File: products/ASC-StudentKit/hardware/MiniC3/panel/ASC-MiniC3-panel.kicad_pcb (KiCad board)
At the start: 2 copper layers, 96 x 100 mm, 156 parts, among them J1_1 PUMP, J1_2 PUMP, J1_3 PUMP, J1_4 PUMP, J1_5 CABLE, J1_6 CABLE, J1_7 CABLE, J1_8 CABLE, J3_1 AUX, J3_2 AUX, J3_3 AUX, J3_4 AUX, J4_1 FLOW, J4_2 FLOW, J4_3 FLOW, J4_4 FLOW, J5_1 I2C, J5_2 I2C, J5_3 I2C, J5_4 I2C, J6_1 RELAY 230V, J6_2 RELAY 230V, J6_3 RELAY 230V, J6_4 RELAY 230V, K1_1 HF46F/005-HS1, K1_2 HF46F/005-HS1, K1_3 HF46F/005-HS1, K1_4 HF46F/005-HS1, Q1_1 AO3400A, Q1_2 AO3400A, Q1_3 AO3400A, Q1_4 AO3400A, Q2_1 AO3400A, Q2_2 AO3400A, Q2_3 AO3400A, Q2_4 AO3400A, U1_1 ESP32-C3 Super Mini, U1_2 ESP32-C3 Super Mini, U1_3 ESP32-C3 Super Mini, U1_4 ESP32-C3 Super Mini, U1_5 AHT20, U1_6 AHT20, U1_7 AHT20, U1_8 AHT20, U2_1 DS1307Z+, U2_2 DS1307Z+, U2_3 DS1307Z+, U2_4 DS1307Z+, Y1_1 32.768k 12.5pF, Y1_2 32.768k 12.5pF, Y1_3 32.768k 12.5pF, Y1_4 32.768k 12.5pF

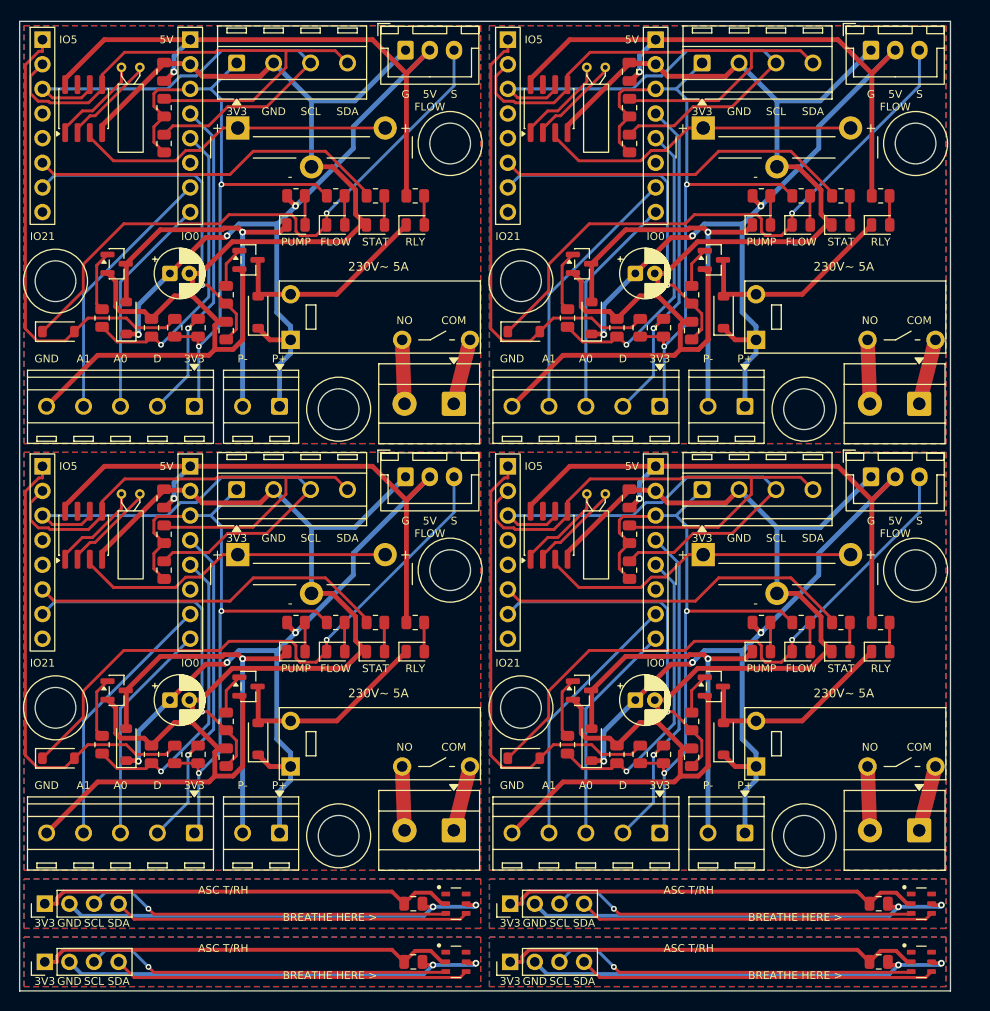
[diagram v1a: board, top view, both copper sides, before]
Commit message: ASC Mini-C3: ULN2003A driver, combo flow connector, assembly markings
- ULN2003A (LCSC C7512) drives the pump (ch 1+2) and the relay (ch 3);
  replaces 2 x AO3400A, 3 x B5819W and 4 resistors, as on FG1
- Flow input: one footprint takes a JST-XH (bench) or a 3.5 mm 3-pole
  screw terminal (FG1 field cable)
- Screw terminals now Phoenix PT-1,5 3.5 mm (KF350 type, library 3D);
  relay output is a pluggable MSTBVA 5.08 header like FG1's
- 1206 LEDs for hand soldering; ref + value labels on every part
  (R3 1K, U3 ULN2003 ...), "1" at IC pin 1, "+" at LED/diode anodes;
  back reads "Agri Sensors and Controls  Oct 2026"
- Re-routed, DRC clean (mains 5 mm), panel and fab regenerated
- Sourcing BOM: 1206 LED and ULN2003A LCSC numbers, CR2032 holder as an
  alternative to the tabbed cell; kit about Rs 967

Co-Authored-By: Claude Opus 5.5 <noreply@anthropic.com>
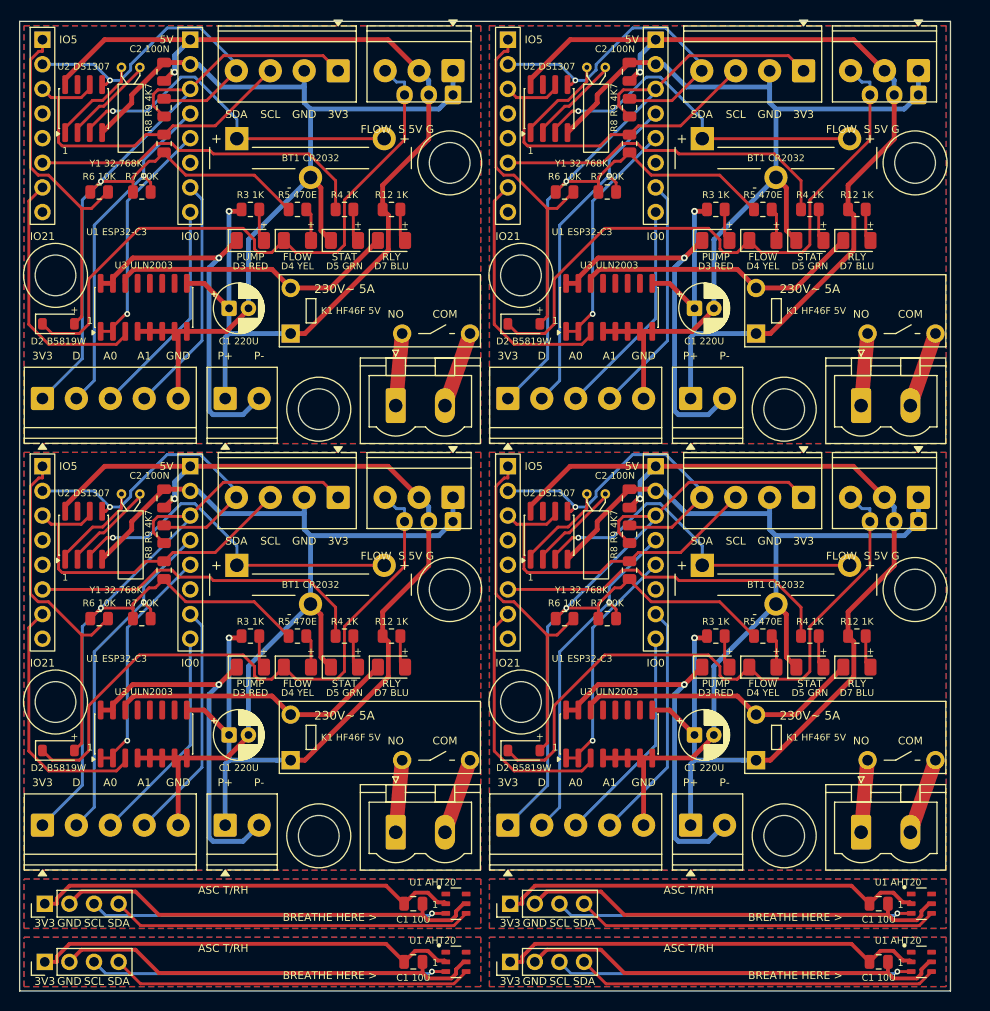
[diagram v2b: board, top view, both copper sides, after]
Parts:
- removed D1_1, D1_2, D1_3, D1_4, D6_1, D6_2, D6_3, D6_4: B5819W, Diode_SMD:D_SOD-123
- removed Q1_1, Q1_2, Q1_3, Q1_4, Q2_1, Q2_2, Q2_3, Q2_4: AO3400A, Package_TO_SOT_SMD:SOT-23
- removed R10_1, R10_2, R10_3, R10_4, R1_1, R1_2, R1_3, R1_4: 100, Resistor_SMD:R_0805_2012Metric
- removed R11_1, R11_2, R11_3, R11_4, R2_1, R2_2, R2_3, R2_4: 100k, Resistor_SMD:R_0805_2012Metric
- added U3_1: ULN2003A, Package_SO:SOIC-16_3.9x9.9mm_P1.27mm, F.Cu at (112.8, 89.5)
- added U3_2: ULN2003A, Package_SO:SOIC-16_3.9x9.9mm_P1.27mm, F.Cu at (160.8, 89.5)
- added U3_3: ULN2003A, Package_SO:SOIC-16_3.9x9.9mm_P1.27mm, F.Cu at (112.8, 133.5)
- added U3_4: ULN2003A, Package_SO:SOIC-16_3.9x9.9mm_P1.27mm, F.Cu at (160.8, 133.5)
- D3_1, D3_2, D3_3, D3_4, D4_1, D4_2, D4_3, D4_4, D5_1, D5_2, D5_3, D5_4, D7_1, D7_2, D7_3, D7_4: footprint LED_SMD:LED_0805_2012Metric -> LED_SMD:LED_1206_3216Metric
- J1_1, J1_2, J1_3, J1_4: footprint TerminalBlock_MetzConnect:TerminalBlock_MetzConnect_Type086_RT03402HBLC_1x02_P3.81mm_Horizontal -> TerminalBlock_Phoenix:TerminalBlock_Phoenix_PT-1,5-2-3.5-H_1x02_P3.50mm_Horizontal
- J3_1, J3_2, J3_3, J3_4: footprint TerminalBlock_MetzConnect:TerminalBlock_MetzConnect_Type086_RT03405HBLC_1x05_P3.81mm_Horizontal -> TerminalBlock_Phoenix:TerminalBlock_Phoenix_PT-1,5-5-3.5-H_1x05_P3.50mm_Horizontal
- J4_1, J4_2, J4_3, J4_4: value FLOW -> FLOW (XH or 3.5 mm); footprint Connector_JST:JST_XH_B3B-XH-A_1x03_P2.50mm_Vertical -> ASC:Flow_XH3_or_PT-1,5-3-3.5mm
- J5_1, J5_2, J5_3, J5_4: footprint TerminalBlock_MetzConnect:TerminalBlock_MetzConnect_Type086_RT03404HBLC_1x04_P3.81mm_Horizontal -> TerminalBlock_Phoenix:TerminalBlock_Phoenix_PT-1,5-4-3.5-H_1x04_P3.50mm_Horizontal
- J6_1, J6_2, J6_3, J6_4: value RELAY 230V -> RELAY 230V (MSTBVA); footprint TerminalBlock_MetzConnect:TerminalBlock_MetzConnect_Type101_RT01602HBWC_1x02_P5.08mm_Horizontal -> Connector_Phoenix_MSTB:PhoenixContact_MSTBVA_2,5_2-G-5,08_1x02_P5.08mm_Vertical
- moved R6_2 16.0 mm to (156.2, 77.6), turned to 0 degrees
- moved R6_4 16.0 mm to (156.2, 121.6), turned to 0 degrees
- moved R6_1 16.0 mm to (108.2, 77.6), turned to 0 degrees
- moved R6_3 16.0 mm to (108.2, 121.6), turned to 0 degrees
- moved J3_2 15.7 mm to (150.3, 98.9), turned to 0 degrees
- moved J3_4 15.7 mm to (150.3, 142.9), turned to 0 degrees
- moved J3_1 15.7 mm to (102.3, 98.9), turned to 0 degrees
- moved J3_3 15.7 mm to (102.3, 142.9), turned to 0 degrees
- moved R7_1 15.2 mm to (112.6, 77.6), turned to 0 degrees
- moved R7_2 15.2 mm to (160.6, 77.6), turned to 0 degrees
- moved R7_3 15.2 mm to (112.6, 121.6), turned to 0 degrees
- moved R7_4 15.2 mm to (160.6, 121.6), turned to 0 degrees
- moved J5_2 10.5 mm to (180.8, 65.1), turned to 180 degrees
- moved J5_4 10.5 mm to (180.8, 109.1), turned to 180 degrees
- moved J5_1 10.5 mm to (132.8, 65.1), turned to 180 degrees
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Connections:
- J6_1 pad 1: B1/RELAY_COM -> B1/RELAY_NO
- J6_1 pad 2: B1/RELAY_NO -> B1/RELAY_COM
- J6_2 pad 1: B2/RELAY_COM -> B2/RELAY_NO
- J6_2 pad 2: B2/RELAY_NO -> B2/RELAY_COM
- J6_3 pad 1: B3/RELAY_COM -> B3/RELAY_NO
- J6_3 pad 2: B3/RELAY_NO -> B3/RELAY_COM
- J6_4 pad 1: B4/RELAY_COM -> B4/RELAY_NO
- J6_4 pad 2: B4/RELAY_NO -> B4/RELAY_COM
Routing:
- net B3/GND: track 129.9 -> 97.4 mm
- net B4/GND: track 129.9 -> 97.4 mm
- net B1/GND: track 129.9 -> 97.4 mm
- net B2/GND: track 129.9 -> 97.4 mm
- net B2/+3V3: track 66.4 -> 88.3 mm, vias 2 -> 1
- net B1/+3V3: track 66.4 -> 88.3 mm, vias 2 -> 1
- net B4/+3V3: track 66.4 -> 88.3 mm, vias 2 -> 1
- net B3/+3V3: track 66.4 -> 88.3 mm, vias 2 -> 1
- net B4/SDA: track 56.0 -> 35.3 mm, vias 0 -> 1
- net B3/SDA: track 56.0 -> 35.3 mm, vias 0 -> 1
- net B2/SDA: track 56.0 -> 35.3 mm, vias 0 -> 1
- net B1/SDA: track 56.0 -> 35.3 mm, vias 0 -> 1
- net B3/+5V: track 132.1 -> 112.9 mm, vias 4 -> 2
- net B4/+5V: track 132.1 -> 112.9 mm, vias 4 -> 2
- net B1/+5V: track 132.1 -> 112.9 mm, vias 4 -> 2
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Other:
- board text added: "+"
- board text added: "1"
- board text added: "Agri Sensors and Controls Oct 2026"
- board text added: "BT1 CR2032"
- board text added: "C1 10U"
- board text added: "C1 220U"
- board text added: "C2 100N"
- board text added: "D2 B5819W"
- board text added: "D3 RED"
- board text added: "D4 YEL"
- board text added: "D5 GRN"
- board text added: "D7 BLU"
- board text added: "FLOW S 5V G"
- board text added: "K1 HF46F 5V"
- board text added: "R12 1K"
- board text added: "R3 1K"
- board text added: "R4 1K"
- board text added: "R5 470E"
- board text added: "R6 10K"
- board text added: "R7 10K"
- board text added: "R8 R9 4K7"
- board text added: "U1 AHT20"
- board text added: "U1 ESP32-C3"
- board text added: "U2 DS1307"
- board text added: "U3 ULN2003"
- board text added: "Y1 32.768K"
- board text removed: "5V"
- board text removed: "Agri Sensors and Controls"
- board text removed: "G"
- board text removed: "MAINS BEFORE OPENING"
- board text removed: "RELAY 230 V: DISCONNECT"
- board text removed: "S"

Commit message: ASC Mini-C3: LED colours, relay header turned, date line
- LEDs: PUMP and RLY yellow (C30584802), STATUS red (C37635751),
  FLOW yellow-green (C28310441, ~2 V: it runs from 3.3 V into the
  sensor output); the Super Mini's blue LED on GPIO8 is the WiFi LED
- Relay MSTBVA header turned 180 so the curved side faces inward, as on
  FG1; pins re-mapped (1 COM, 2 NO), mains tracks re-drawn, 5.00 mm
- Back silkscreen: "Oct 2026" on its own line
- Re-routed, DRC clean; panel, fab, BOM/CPL and sourcing regenerated

Co-Authored-By: Claude Opus 5.5 <noreply@anthropic.com>
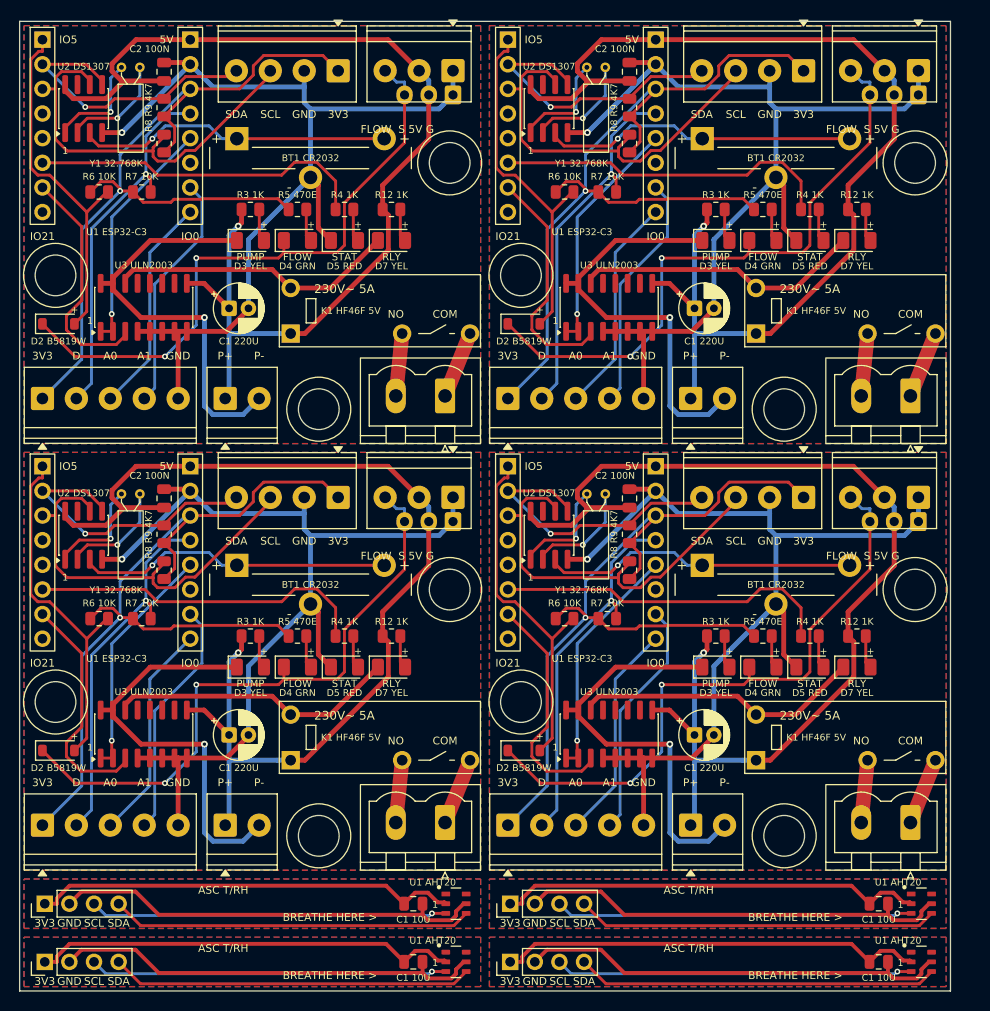
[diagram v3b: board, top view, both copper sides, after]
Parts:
- D3_1, D3_2, D3_3, D3_4: value PUMP red -> PUMP yellow
- D4_1, D4_2, D4_3, D4_4: value FLOW yellow -> FLOW yellow-green
- D5_1, D5_2, D5_3, D5_4: value STATUS green -> STATUS red
- D7_1, D7_2, D7_3, D7_4: value RELAY blue -> RELAY yellow
- moved J6_1 5.19 mm to (143.9, 98.6), turned to 180 degrees
- moved J6_2 5.19 mm to (191.9, 98.6), turned to 180 degrees
- moved J6_3 5.19 mm to (143.9, 142.6), turned to 180 degrees
- moved J6_4 5.19 mm to (191.9, 142.6), turned to 180 degrees
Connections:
- J6_1 pad 1: B1/RELAY_NO -> B1/RELAY_COM
- J6_1 pad 2: B1/RELAY_COM -> B1/RELAY_NO
- J6_2 pad 1: B2/RELAY_NO -> B2/RELAY_COM
- J6_2 pad 2: B2/RELAY_COM -> B2/RELAY_NO
- J6_3 pad 1: B3/RELAY_NO -> B3/RELAY_COM
- J6_3 pad 2: B3/RELAY_COM -> B3/RELAY_NO
- J6_4 pad 1: B4/RELAY_NO -> B4/RELAY_COM
- J6_4 pad 2: B4/RELAY_COM -> B4/RELAY_NO
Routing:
- net B4/SCL: track 35.9 -> 42.0 mm
- net B2/SCL: track 35.9 -> 42.0 mm
- net B3/SCL: track 35.9 -> 42.0 mm
- net B1/SCL: track 35.9 -> 42.0 mm
- net B3/PUMP_N: track 38.4 -> 43.3 mm
- net B4/PUMP_N: track 38.4 -> 43.3 mm
- net B1/PUMP_N: track 38.4 -> 43.3 mm
- net B2/PUMP_N: track 38.4 -> 43.3 mm
- net B3/SDA: track 35.3 -> 30.7 mm
- net B1/SDA: track 35.3 -> 30.7 mm
- net B4/SDA: track 35.3 -> 30.7 mm
- net B2/SDA: track 35.3 -> 30.7 mm
- net B4/VBAT: track 36.8 -> 32.6 mm
- net B2/VBAT: track 36.8 -> 32.6 mm
- net B3/VBAT: track 36.8 -> 32.6 mm
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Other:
- board text added: "Agri Sensors and Controls"
- board text added: "D3 YEL"
- board text added: "D4 GRN"
- board text added: "D5 RED"
- board text added: "D7 YEL"
- board text added: "Oct 2026"
- board text removed: "Agri Sensors and Controls Oct 2026"
- board text removed: "D3 RED"
- board text removed: "D4 YEL"
- board text removed: "D5 GRN"
- board text removed: "D7 BLU"
